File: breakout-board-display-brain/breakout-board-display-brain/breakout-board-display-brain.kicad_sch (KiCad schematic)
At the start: 7 parts, among them J1 Conn_01x19_Socket, J2 Conn_01x19_Socket, J3 Conn_01x16_Female, J4 Conn_01x02_Socket, SW1 RotaryEncoder_Switch

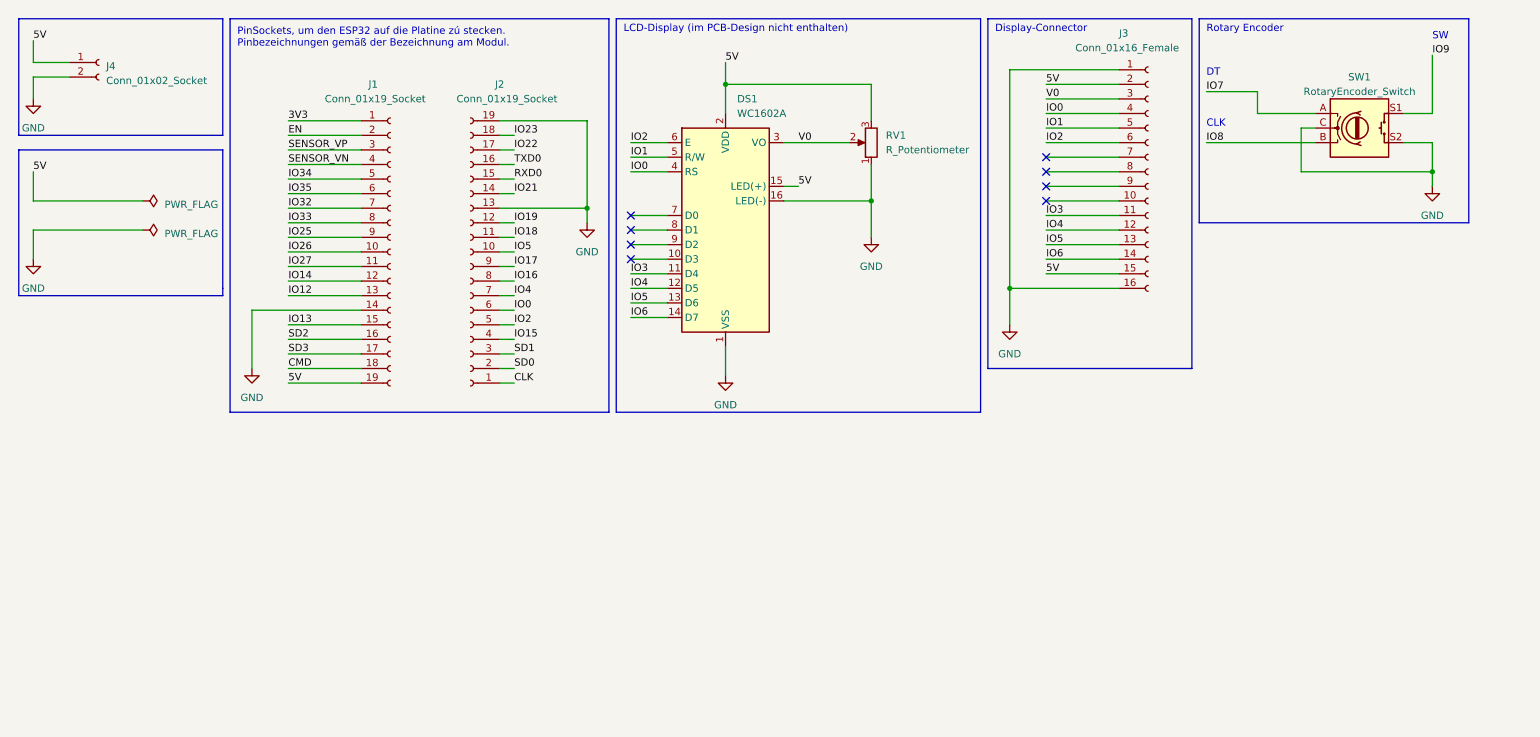
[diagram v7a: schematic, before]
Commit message: changes made to attiny and display brain breakout board
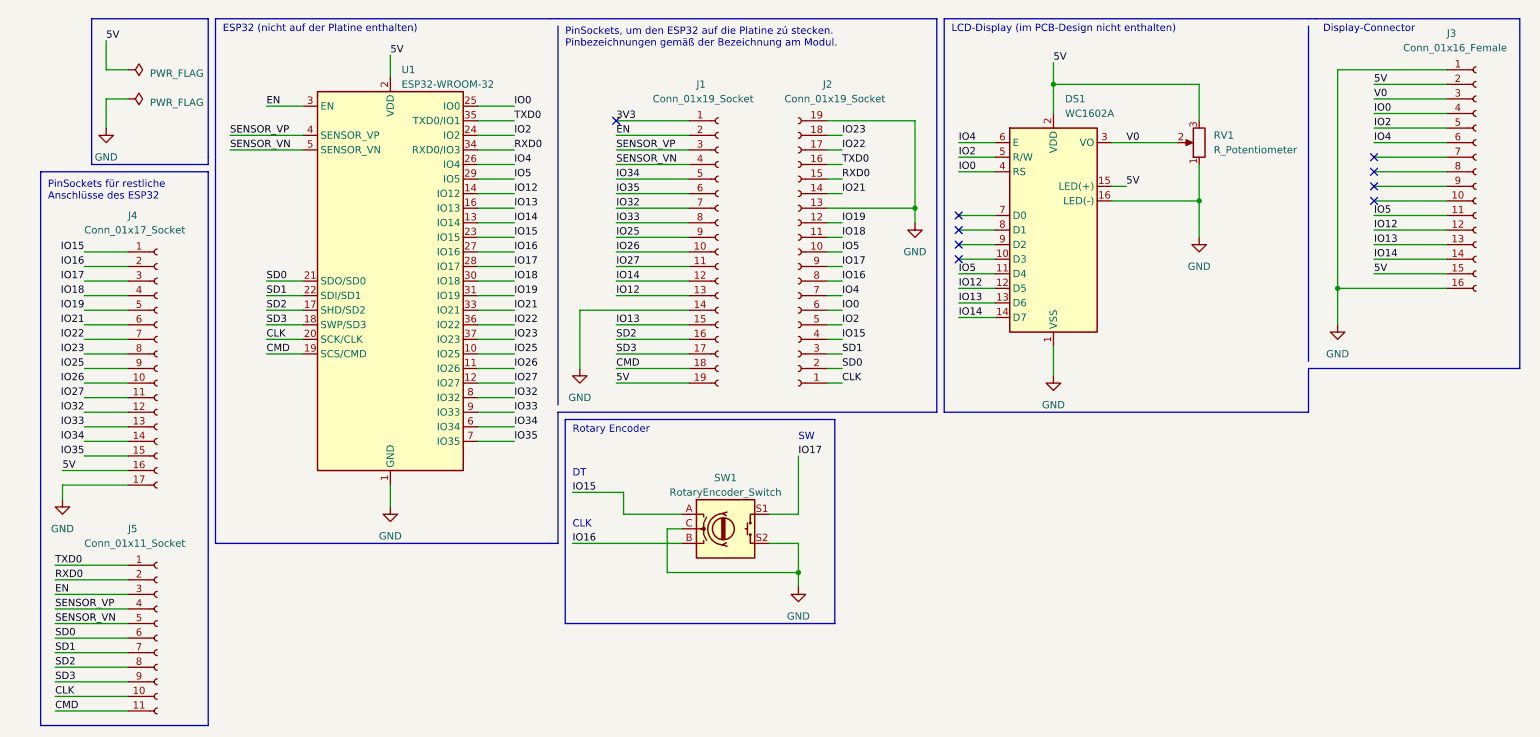
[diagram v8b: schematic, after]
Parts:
- removed J4: Conn_01x02_Socket, Connector_PinSocket_2.54mm:PinSocket_1x02_P2.54mm_Vertical, symbol Connector:Conn_01x02_Socket
- added J4: Conn_01x17_Socket, symbol Connector:Conn_01x17_Socket
- added J5: Conn_01x11_Socket, symbol Connector:Conn_01x11_Socket
- added U1: ESP32-WROOM-32, RF_Module:ESP32-WROOM-32, symbol RF_Module:ESP32-WROOM-32
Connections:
- net IO1 is gone; now on net IO2: DS1.5 (R/W), J3.5 (Pin_5)
- net IO3 is gone; now on net IO5: DS1.11 (D4), J3.11 (Pin_11)
- net IO6 is gone; now on net IO14: DS1.14 (D7), J3.14 (Pin_14)
- net IO7 is gone; now on net IO15: SW1.A
- net IO8 is gone; now on net IO16: SW1.B
- net IO9 is gone; now on net IO17: SW1.S1
- net 5V: now also J4.16 (Pin_16), U1.2 (VDD)
- net CLK: now also J5.10 (Pin_10), U1.20 (SCK/CLK)
- net CMD: now also J5.11 (Pin_11), U1.19 (SCS/CMD)
- net EN: now also J5.3 (Pin_3), U1.3 (EN)
- net GND: now also J4.17 (Pin_17), U1.1 (GND), U1.15 (GND), U1.38 (GND), U1.39 (GND)
- net IO0: now also U1.25 (IO0)
- net IO12: now also DS1.12 (D5), J3.12 (Pin_12), U1.14 (IO12)
- net IO13: now also DS1.13 (D6), J3.13 (Pin_13), U1.16 (IO13)
- net IO14: now also U1.13 (IO14)
- net IO15: now also J4.1 (Pin_1), U1.23 (IO15)
- net IO16: now also J4.2 (Pin_2), U1.27 (IO16)
- net IO17: now also J4.3 (Pin_3), U1.28 (IO17)
- net IO18: now also J4.4 (Pin_4), U1.30 (IO18)
- net IO19: now also J4.5 (Pin_5), U1.31 (IO19)
- net IO2: now also U1.24 (IO2); no longer DS1.6 (E), J3.6 (Pin_6)
- net IO21: now also J4.6 (Pin_6), U1.33 (IO21)
- net IO22: now also J4.7 (Pin_7), U1.36 (IO22)
- net IO23: now also J4.8 (Pin_8), U1.37 (IO23)
- net IO25: now also J4.9 (Pin_9), U1.10 (IO25)
- net IO26: now also J4.10 (Pin_10), U1.11 (IO26)
- net IO27: now also J4.11 (Pin_11), U1.12 (IO27)
- net IO32: now also J4.12 (Pin_12), U1.8 (IO32)
- net IO33: now also J4.13 (Pin_13), U1.9 (IO33)
- net IO34: now also J4.14 (Pin_14), U1.6 (IO34)
- net IO35: now also J4.15 (Pin_15), U1.7 (IO35)
- net IO4: now also DS1.6 (E), J3.6 (Pin_6), U1.26 (IO4); no longer DS1.12 (D5), J3.12 (Pin_12)
- net IO5: now also U1.29 (IO5); no longer DS1.13 (D6), J3.13 (Pin_13)
- net RXD0: now also J5.2 (Pin_2), U1.34 (RXD0/IO3)
- net SD0: now also J5.6 (Pin_6), U1.21 (SDO/SD0)
- net SD1: now also J5.7 (Pin_7), U1.22 (SDI/SD1)
- net SD2: now also J5.8 (Pin_8), U1.17 (SHD/SD2)
- net SD3: now also J5.9 (Pin_9), U1.18 (SWP/SD3)
- net SENSOR_VN: now also J5.5 (Pin_5), U1.5 (SENSOR_VN)
- net SENSOR_VP: now also J5.4 (Pin_4), U1.4 (SENSOR_VP)
- net TXD0: now also J5.1 (Pin_1), U1.35 (TXD0/IO1)
- no-connect marks 8 -> 9
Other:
- note added: "ESP32 (nicht auf der Platine enthalten)"
- note added: "PinSockets für restliche Anschlüsse des ESP32"
- moved on the sheet: DS1, J1, J2, J3, RV1, SW1
